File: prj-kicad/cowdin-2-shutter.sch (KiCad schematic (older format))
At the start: 8 parts, among them P1 CONN_3, P2 CONN_3, P3 CONN_3, P4 CONN_3

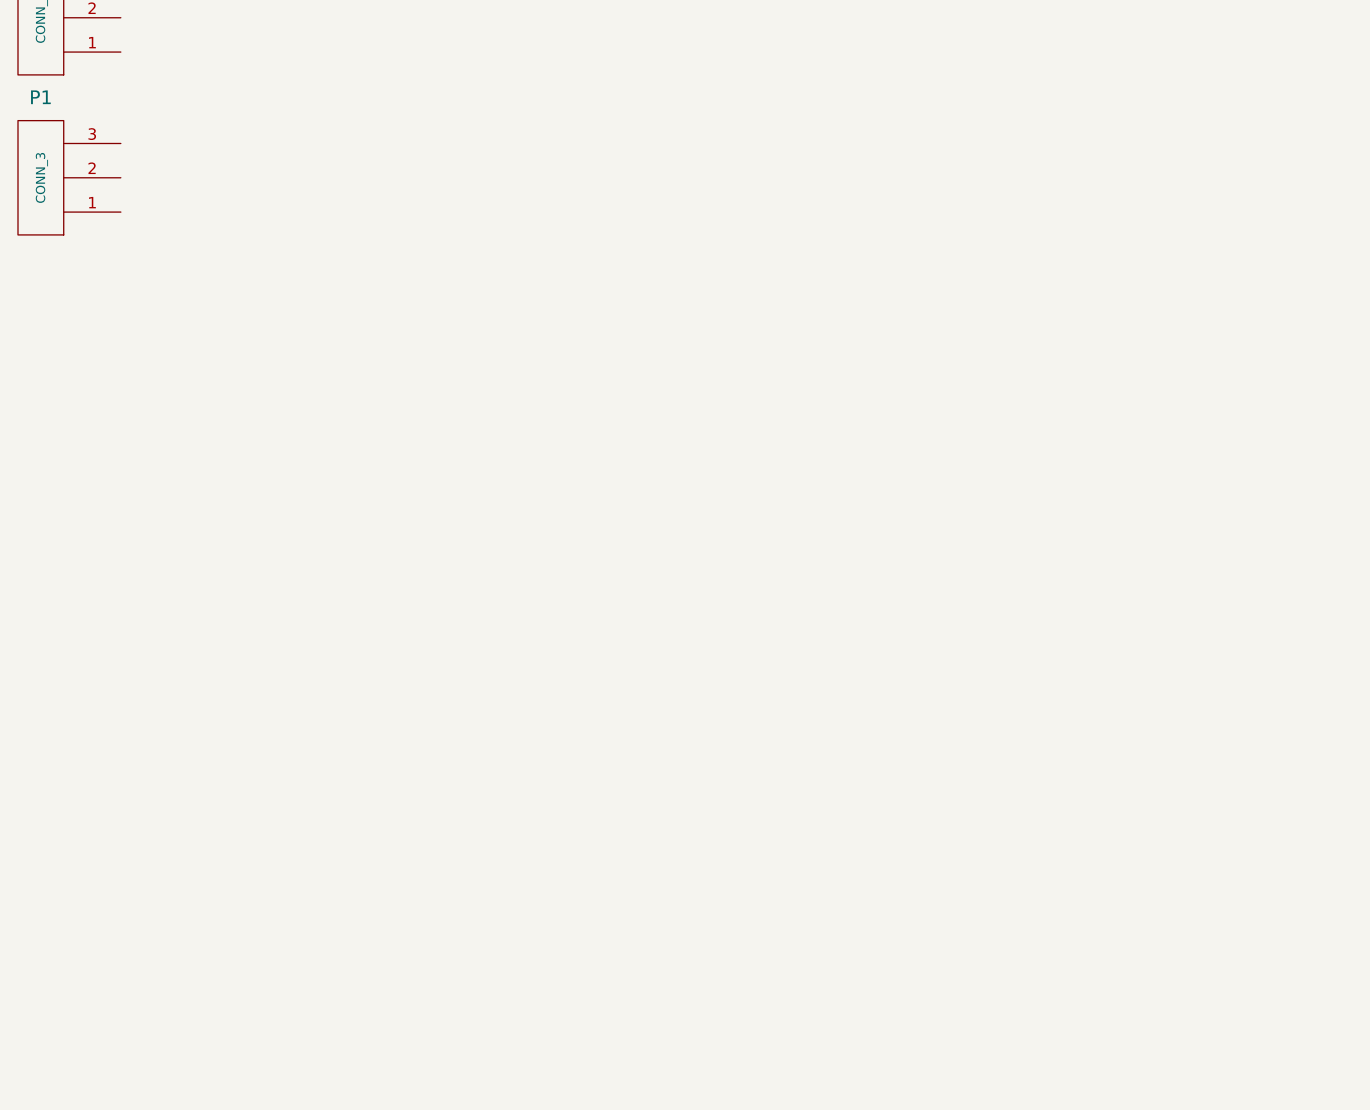
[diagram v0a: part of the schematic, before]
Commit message: = ADD: Insert power supply for wide VIN (5-40V) to 5V internal
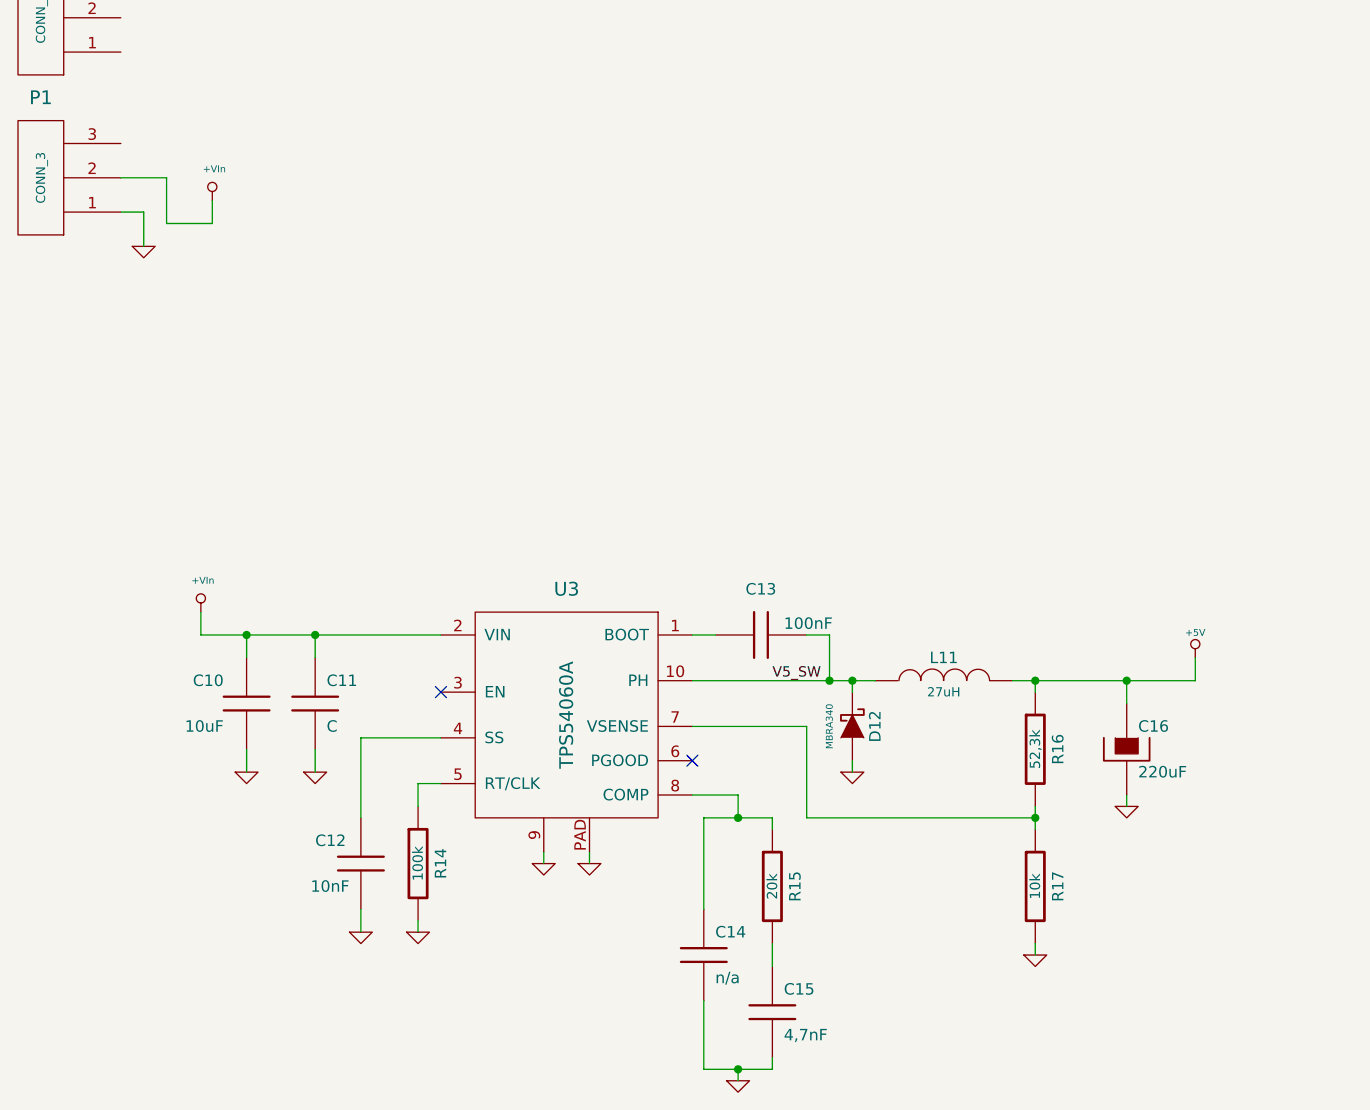
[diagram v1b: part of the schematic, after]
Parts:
- added C10: 10uF, cowdin-2-shutter:SMD1210, symbol cowdin-2-shutter:C
- added C11: C, cowdin-2-shutter:SMD1210, symbol cowdin-2-shutter:C
- added C12: 10nF, cowdin-2-shutter:SMD0603, symbol cowdin-2-shutter:C
- added C13: 100nF, cowdin-2-shutter:SMD0603, symbol cowdin-2-shutter:C
- added C14: n/a, cowdin-2-shutter:SMD0603, symbol cowdin-2-shutter:C
- added C15: 4,7nF, cowdin-2-shutter:SMD0603, symbol cowdin-2-shutter:C
- added C16: 220uF, cowdin-2-shutter:C_TPB_D4, symbol cowdin-2-shutter:CP
- added D12: MBRA340, cowdin-2-shutter:DO214AC, symbol cowdin-2-shutter:D_Schottky
- added L11: 27uH, cowdin-2-shutter:I_MSS1048, symbol cowdin-2-shutter:INDUCTOR
- added R14: 100k, cowdin-2-shutter:SMD0603, symbol cowdin-2-shutter:R
- added R15: 20k, cowdin-2-shutter:SMD0603, symbol cowdin-2-shutter:R
- added R16: 52,3k, cowdin-2-shutter:SMD0603, symbol cowdin-2-shutter:R
- added R17: 10k, cowdin-2-shutter:SMD0603, symbol cowdin-2-shutter:R
- added U3: TPS54060A, cowdin-2-shutter:MSOP10p, symbol cowdin-2-shutter:TPS54060A
- P1, P3: footprint (none) -> cowdin-2-shutter:CONN_MC000035
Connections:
- net GND: now reaches P1.1 (P1)
- net GND: now also C10.2, C11.2, C12.2, C14.2, C15.2, C16.2, D12.1 (A), R14.2, R17.2, U3.9, U3.PAD
- net VIn: now reaches P1.2 (P2)
- net VIn: now also C10.1, C11.1, U3.2 (VIN)
- new net: C13.1, U3.1 (BOOT)
- new net: C12.1, U3.4 (SS)
- new net: R14.1, U3.5 (RT/CLK)
- new net: R16.2, R17.1, U3.7 (VSENSE)
- new net: C14.1, R15.1, U3.8 (COMP)
- new net: C15.1, R15.2
- new net 5V: C16.1, L11.2, R16.1
- new net V5_SW: C13.2, D12.2 (K), L11.1, U3.10 (PH)
- no-connect marks 1 -> 3

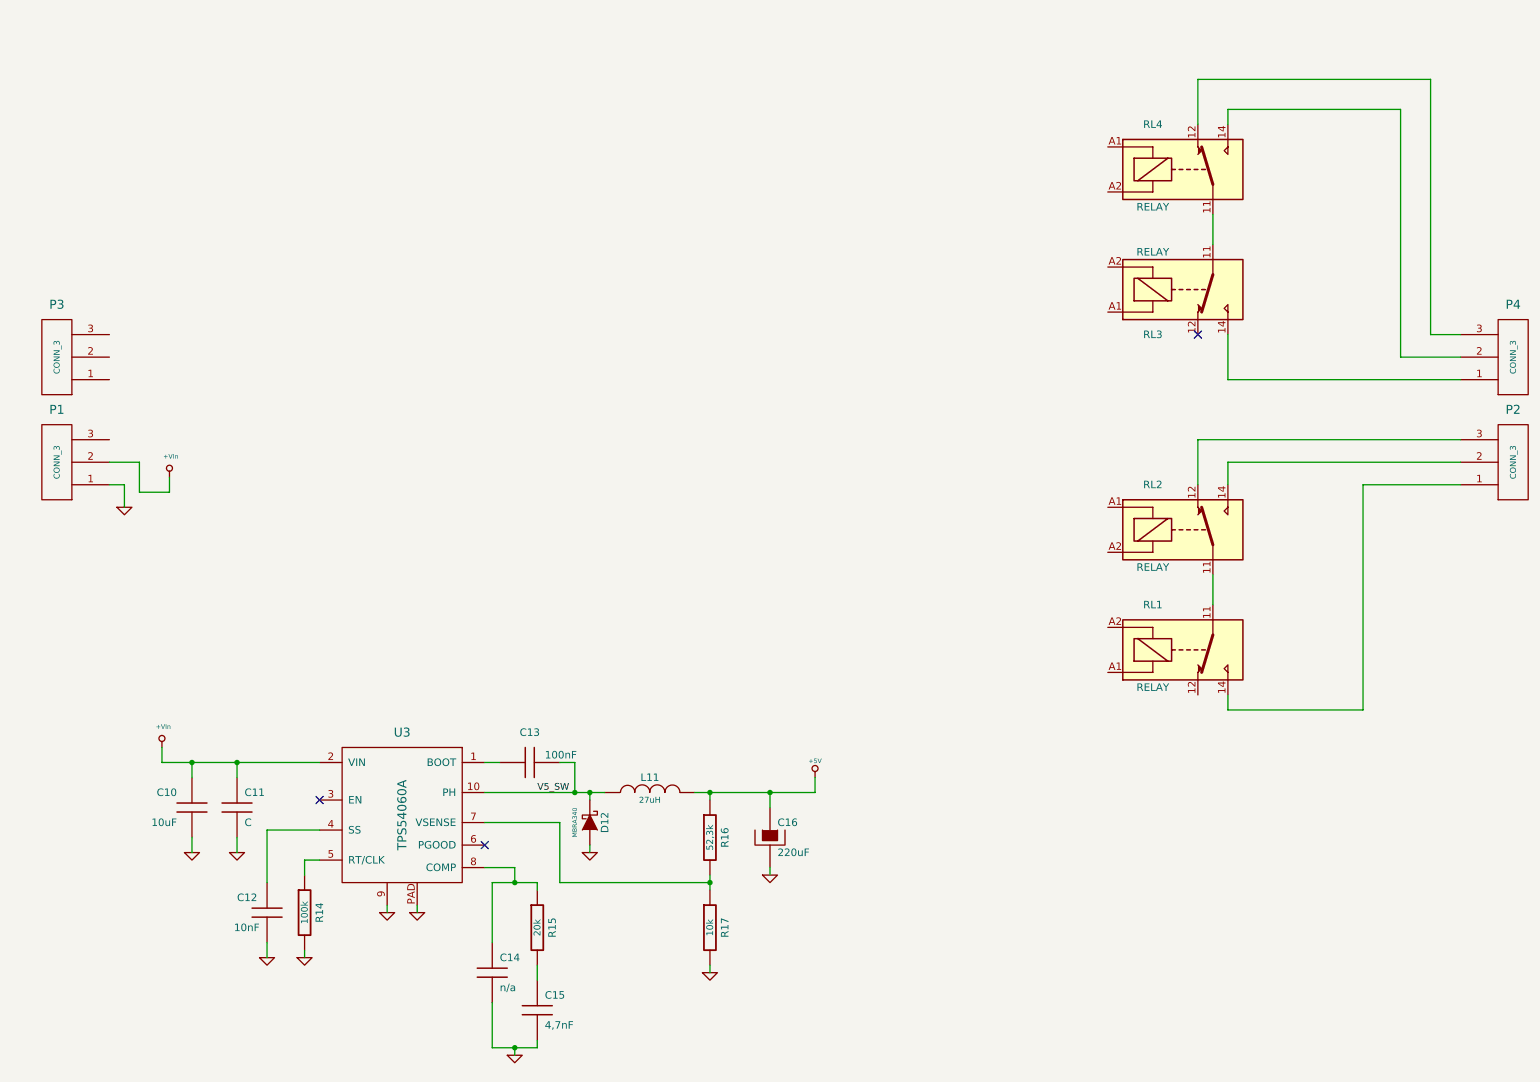
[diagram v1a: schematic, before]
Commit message: = ADD: Insert processor and CAN interface (sch & routing)
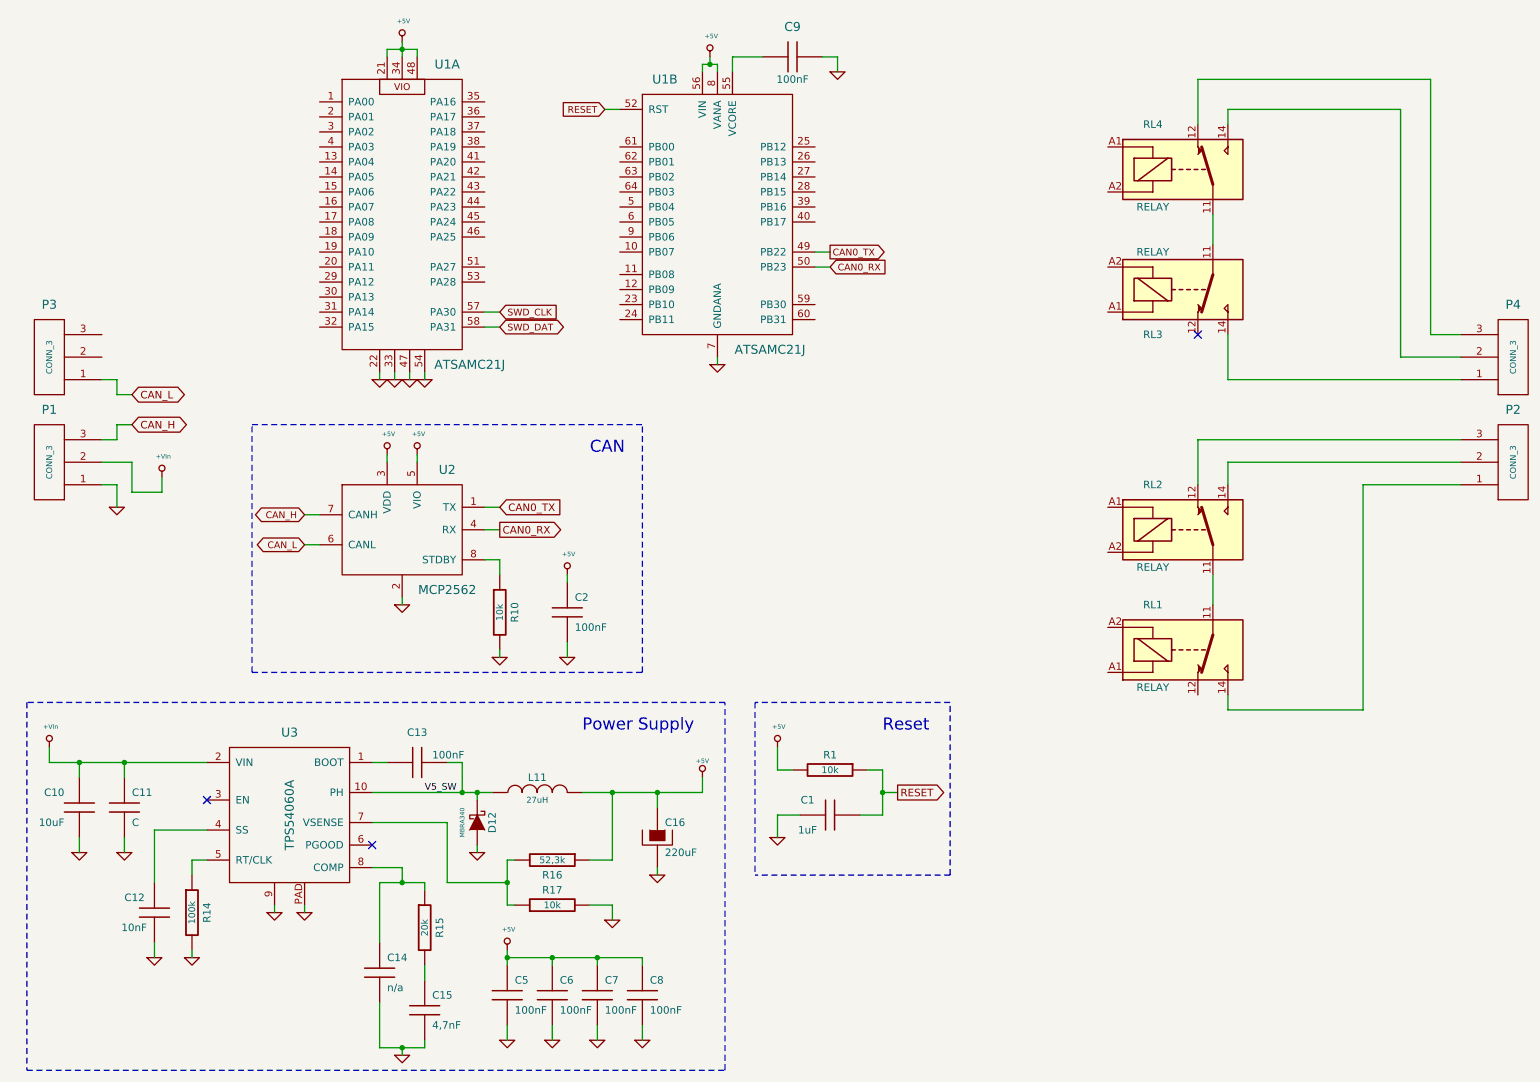
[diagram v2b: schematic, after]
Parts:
- added C1: 1uF, cowdin-2-shutter:SMD0603, symbol cowdin-2-shutter:C
- added C2, C5, C6, C7, C8, C9: 100nF, cowdin-2-shutter:SMD0603, symbol cowdin-2-shutter:C
- added R1, R10: 10k, cowdin-2-shutter:SMD0603, symbol cowdin-2-shutter:R
- added U1: ATSAMC21J, cowdin-2-shutter:TQFP64, symbol cowdin-2-shutter:ATSAMC21J
- added U2: MCP2562, cowdin-2-shutter:SOIC-8E, symbol cowdin-2-shutter:MCP2562
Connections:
- net 5V: now also C2.1, C5.1, C6.1, C7.1, C8.1, R1.2, U1.21, U1.34, U1.48, U1.56 (VIN), U1.8 (VANA), U2.3 (VDD), U2.5 (VIO)
- net GND: now also C1.2, C2.2, C5.2, C6.2, C7.2, C8.2, C9.1, R10.2, U1.22, U1.33, U1.47, U1.54, U1.7 (GNDANA), U2.2
- net CAN_H: now reaches P1.3 (P3)
- net CAN_H: now also U2.7 (CANH)
- net CAN_L: now reaches P3.1 (P1)
- net CAN_L: now also U2.6 (CANL)
- new net: C9.2, U1.55 (VCORE)
- new net: R10.1, U2.8 (STDBY)
- new net CAN0_RX: U1.50 (PB23), U2.4 (RX)
- new net CAN0_TX: U1.49 (PB22), U2.1 (TX)
- new net RESET: C1.1, R1.1, U1.52 (RST)
- new net SWD_CLK: U1.57 (PA30)
- new net SWD_DAT: U1.58 (PA31)
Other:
- note added: "CAN"
- note added: "Power Supply"
- note added: "Reset"
- moved on the sheet: C10, C11, C12, C13, C14, C15, C16, D12, L11, P1, P3, R14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

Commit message: = ADD: Insert input and output interfaces
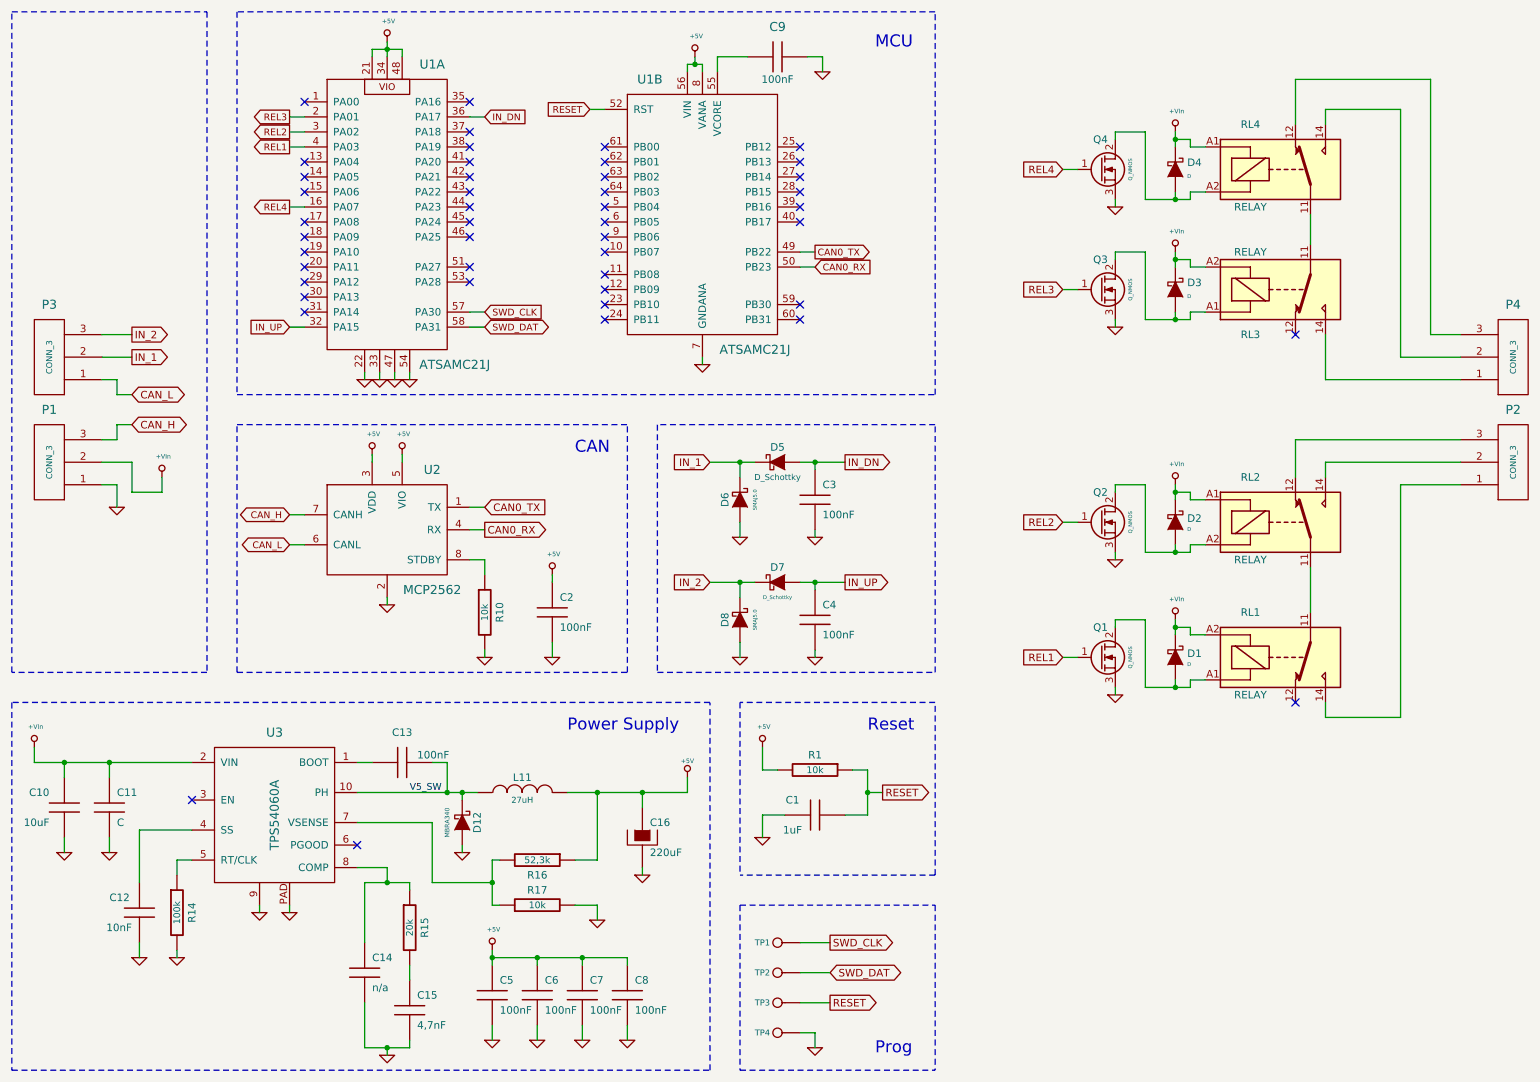
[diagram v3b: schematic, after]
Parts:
- added C3, C4: 100nF, cowdin-2-shutter:SMD0603, symbol cowdin-2-shutter:C
- added D1, D2, D3, D4: D, cowdin-2-shutter:SOD-123, symbol cowdin-2-shutter:D_Schottky
- added D5, D7: D_Schottky, cowdin-2-shutter:SOD-123, symbol cowdin-2-shutter:D_Schottky
- added D6, D8: SMAJ5.0, cowdin-2-shutter:DO214AC, symbol cowdin-2-shutter:D_Schottky
- added Q1, Q2, Q3, Q4: Q_NMOS, cowdin-2-shutter:SOT23-3, symbol cowdin-2-shutter:Q_NMOS
- added TP1, TP2, TP3, TP4: CONN_1, cowdin-2-shutter:TP_SMD, symbol cowdin-2-shutter:CONN_1
- P2, P4: footprint cowdin-2-shutter:CONN_691411710003 -> cowdin-2-shutter:CONN_MC000035
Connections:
- net GND: now also C3.2, C4.2, D6.1 (A), D8.1 (A), Q1.3 (S), Q2.3 (S), Q3.3 (S), Q4.3 (S), TP4.1
- net RESET: now also TP3.1
- net SWD_CLK: now also TP1.1
- net SWD_DAT: now also TP2.1
- net VIn: now also RL1.A2, RL2.A1, RL3.A2, RL4.A1, D1.2 (K), D2.2 (K), D3.2 (K), D4.2 (K)
- net IN_1: now reaches P3.2 (P2)
- net IN_1: now also D5.2 (K), D6.2 (K)
- net IN_2: now reaches P3.3 (P3)
- net IN_2: now also D7.2 (K), D8.2 (K)
- net at RL1.A1: now also D1.1 (A), Q1.2 (D)
- net at RL2.A2: now also D2.1 (A), Q2.2 (D)
- net at RL3.A1: now also D3.1 (A), Q3.2 (D)
- net at RL4.A2: now also D4.1 (A), Q4.2 (D)
- net REL4: now reaches U1.16 (PA07)
- net REL4: now also Q4.1 (G)
- net REL3: now reaches U1.2 (PA01)
- net REL3: now also Q3.1 (G)
- net REL2: now reaches U1.3 (PA02)
- net REL2: now also Q2.1 (G)
- net IN_UP: now reaches U1.32 (PA15)
- net IN_UP: now also C4.1, D7.1 (A)
- net IN_DN: now reaches U1.36 (PA17)
- net IN_DN: now also C3.1, D5.1 (A)
- net REL1: now reaches U1.4 (PA03)
- net REL1: now also Q1.1 (G)
- no-connect marks 3 -> 46
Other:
- note added: "MCU"
- note added: "Prog"
- moved on the sheet: C1, C10, C11, C12, C13, C14, C15, C16, C2, C5, C6, C7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
